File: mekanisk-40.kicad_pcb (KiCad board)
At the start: 2 copper layers, 247.7 x 76.2 mm, 129 parts, among them J2 USB_C_Receptacle_USB2.0, SW1 RST, SW2 RST, U1 USBLC6-2SC6, U2 XC6206PxxxMR-Regulator_Linear, U3 STM32F072C8Tx

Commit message: first full design
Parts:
- removed SW2: RST, Button_Switch_SMD:SW_SPST_SKQG_WithoutStem
- added C11: 4.7u, Capacitor_SMD:C_0603_1608Metric, B.Cu at (64.3, 84.9)
- added Q1: 2N7002, Package_TO_SOT_SMD:SOT-23, B.Cu at (69.1, 84.9)
- added R4: 10k, Resistor_SMD:R_0603_1608Metric, B.Cu at (70.6, 80.2)
- added R5: 100k, Resistor_SMD:R_0603_1608Metric, B.Cu at (65.9, 84.9)
- C10: value 100nF -> 1u
- moved R3 121.5 mm to (67.5, 77.8), turned to 135 degrees
- moved C8 120.7 mm to (70.6, 77.5), turned to -135 degrees
- moved SW1 118.4 mm to (69.1, 89.7), turned to 180 degrees
- moved C1 116.4 mm to (56.4, 53.0)
- moved U2 116.4 mm to (56.4, 56.1)
- moved C6 115.5 mm to (67.5, 63.5), turned to 135 degrees
- moved U3 112.7 mm to (70.6, 69.8), turned to 135 degrees
- moved C4 112.7 mm to (62.7, 67.5)
- moved C5 112.7 mm to (62.7, 69.1)
- moved C2 110.3 mm to (62.7, 64.3)
- moved C3 110.2 mm to (62.7, 65.9)
- moved C10 110.1 mm to (70.6, 81.8), turned to 180 degrees
- moved C9 109.7 mm to (78.6, 70.6)
- moved C7 106.8 mm to (78.6, 69.1), turned to 0 degrees
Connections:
- SW1 pad 1: +3V3 -> BOOT0
- SW1 pad 2: BOOT0 -> +3V3
- U3 pad 11: COL7 -> unconnected-(U3-PA1-Pad11)
- U3 pad 12: COL6 -> unconnected-(U3-PA2-Pad12)
- U3 pad 13: COL5 -> unconnected-(U3-PA3-Pad13)
- U3 pad 14: COL4 -> unconnected-(U3-PA4-Pad14)
- U3 pad 15: COL3 -> unconnected-(U3-PA5-Pad15)
- U3 pad 16: COL2 -> unconnected-(U3-PA6-Pad16)
- U3 pad 19: ROW2 -> unconnected-(U3-PB1-Pad19)
- U3 pad 2: unconnected-(U3-PC13-Pad2) -> COL6
- U3 pad 20: ROW3 -> unconnected-(U3-PB2-Pad20)
- U3 pad 21: ROW0 -> unconnected-(U3-PB10-Pad21)
- U3 pad 22: ROW1 -> unconnected-(U3-PB11-Pad22)
- U3 pad 3: unconnected-(U3-PC14-Pad3) -> COL5
- U3 pad 37: unconnected-(U3-PA14-Pad37) -> ROW1
- U3 pad 38: unconnected-(U3-PA15-Pad38) -> ROW0
- U3 pad 39: unconnected-(U3-PB3-Pad39) -> ROW3
- U3 pad 4: unconnected-(U3-PC15-Pad4) -> COL4
- U3 pad 40: COL11 -> ROW2
- U3 pad 41: COL10 -> COL11
- U3 pad 42: COL9 -> COL10
- U3 pad 43: COL8 -> COL9
- U3 pad 45: unconnected-(U3-PB8-Pad45) -> COL8
- U3 pad 46: unconnected-(U3-PB9-Pad46) -> COL7
- U3 pad 5: unconnected-(U3-PF0-Pad5) -> COL3
- U3 pad 6: unconnected-(U3-PF1-Pad6) -> COL2
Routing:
- net D_N: track 148.7 -> 29.7 mm
- net D_P: track 147.3 -> 28.7 mm
- net +5V: track 131.7 -> 15.1 mm
- net COL10: track 110.9 -> 226.4 mm
- net COL9: track 90.6 -> 205.9 mm
- net COL11: track 150.2 -> 265.2 mm
- net COL0: track 231.4 -> 120.7 mm, vias 1 -> 0
- net COL1: track 193.5 -> 84.0 mm
- net COL2: track 175.2 -> 68.9 mm
- net COL8: track 78.5 -> 184.9 mm
- net COL7: track 59.8 -> 143.3 mm
- net COL3: track 132.7 -> 67.6 mm
- net ROW2: track 404.2 -> 455.3 mm
- net COL6: track 107.9 -> 158.8 mm
- net ROW3: track 427.9 -> 473.9 mm
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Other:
- board text added: "2.25U"
- board text added: "2.75U"
- board text added: "6.25U"
- board text added: "mekanisk40"
- board text added: "push - reset hold - boot"
- board text removed: "BOOT"
- board text removed: "RESET"

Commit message: backup
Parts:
- moved C1 0.71 mm to (57.1, 53.0)
- moved U2 0.71 mm to (57.1, 56.1)
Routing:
- net COL11: track 265.2 -> 261.6 mm
- net ROW1: track 443.2 -> 441.0 mm
- net +3V3: track 90.7 -> 88.7 mm
- net BOOT0: track 36.4 -> 35.1 mm
- net COL5: track 106.1 -> 105.3 mm
- net COL4: track 107.3 -> 106.5 mm

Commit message: slight routing cleanup
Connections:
- U3 pad 17: COL1 -> unconnected-(U3-PA7-Pad17)
- U3 pad 18: COL0 -> unconnected-(U3-PB0-Pad18)
- U3 pad 21: unconnected-(U3-PB10-Pad21) -> COL1
- U3 pad 22: unconnected-(U3-PB11-Pad22) -> COL0
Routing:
- net GND: track 92.4 -> 95.0 mm, vias 3 -> 2
- net COL0: track 120.7 -> 118.3 mm
- net COL1: track 84.0 -> 81.6 mm

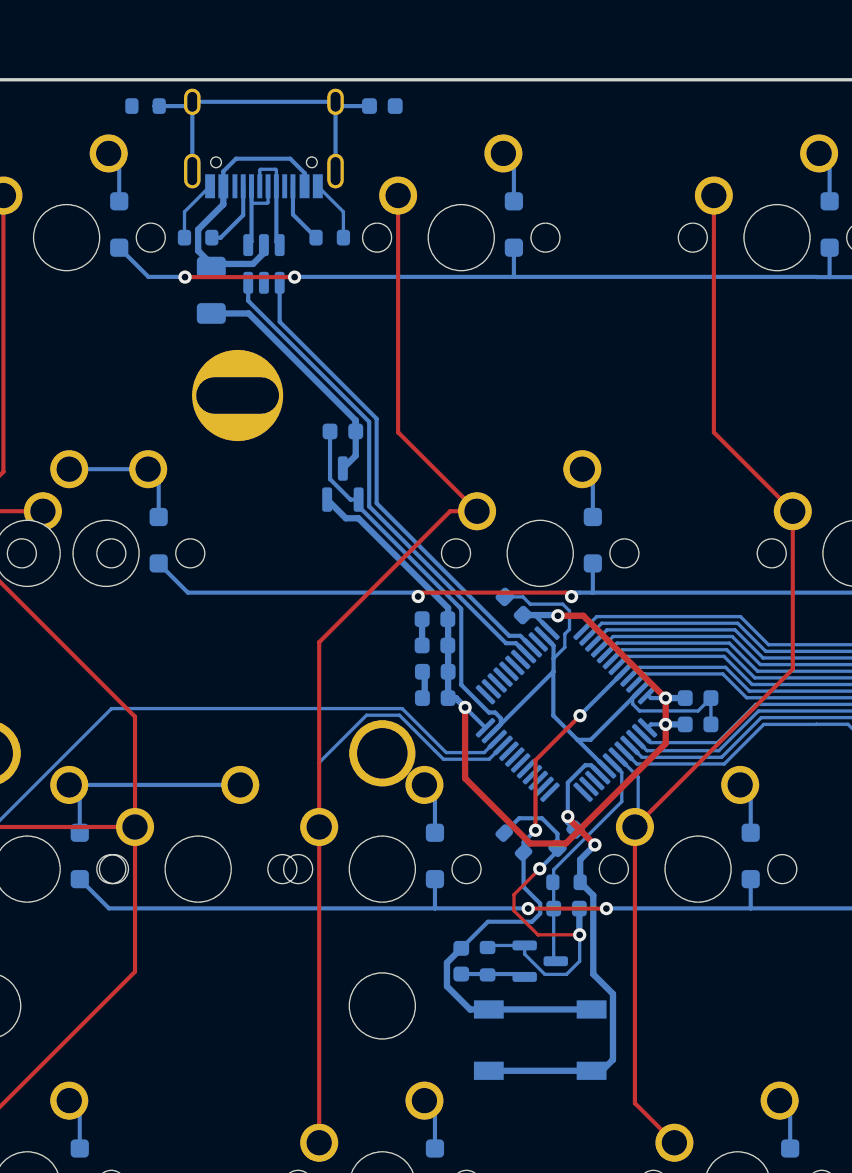
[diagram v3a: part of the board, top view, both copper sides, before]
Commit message: component placement
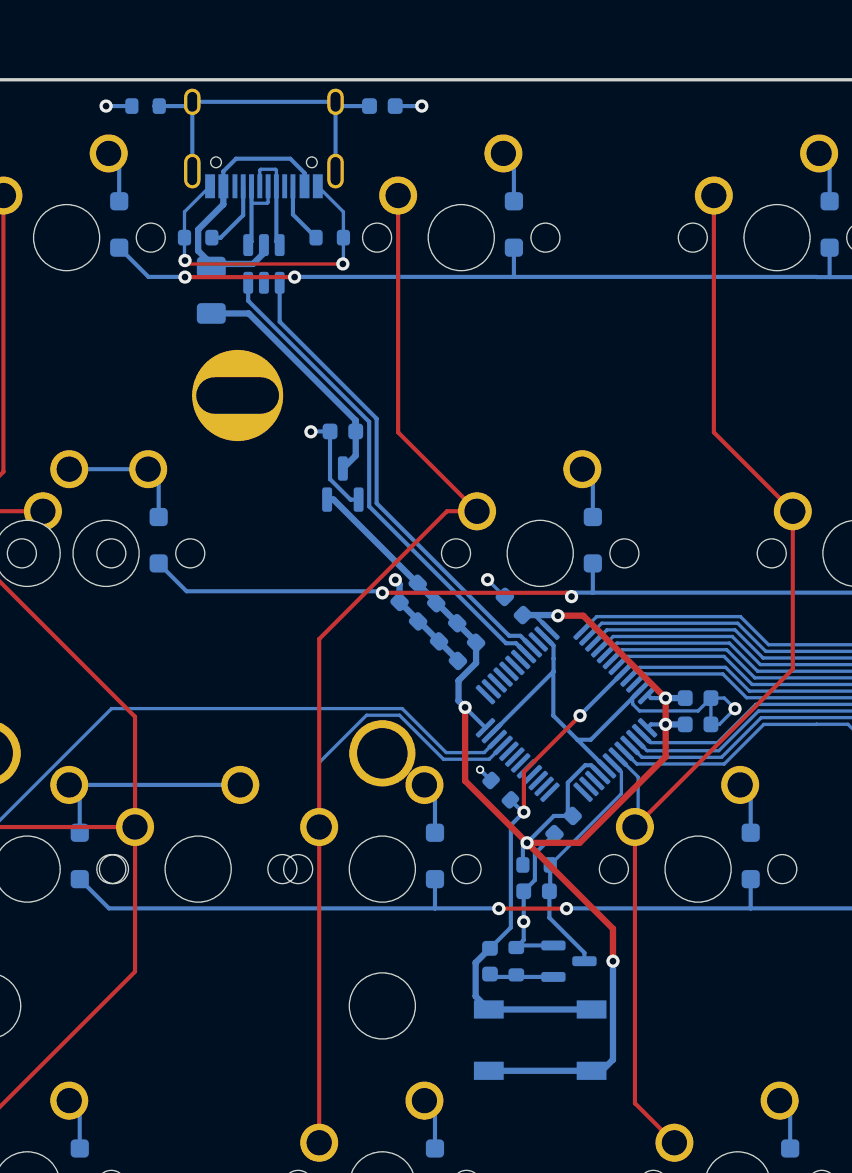
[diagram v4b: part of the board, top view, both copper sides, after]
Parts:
- moved C5 3.38 mm to (64.6, 66.3), turned to -135 degrees
- moved R3 3.27 mm to (66.7, 74.6)
- moved C4 2.50 mm to (63.5, 65.1), turned to -135 degrees
- moved C2 2.25 mm to (61.1, 62.7), turned to 45 degrees
- moved R4 2.09 mm to (68.8, 79.1), turned to 0 degrees
- moved C10 2.09 mm to (68.8, 80.7), turned to 0 degrees
- moved C3 2.05 mm to (62.2, 63.9), turned to -135 degrees
- moved C11 1.73 mm to (66.0, 84.9)
- moved R5 1.73 mm to (67.6, 84.9)
- moved Q1 1.73 mm to (70.8, 84.9)
- moved C8 0.84 mm to (70.5, 76.7)
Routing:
- net GND: track 95.0 -> 82.4 mm, vias 2 -> 10
- net BOOT0: track 35.1 -> 31.8 mm
- net +3V3: track 88.7 -> 91.9 mm
- net NRST: track 14.0 -> 14.9 mm
